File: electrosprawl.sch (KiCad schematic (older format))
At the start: 49 parts, among them J1 3.3v, J2 Conn_02x08_Counter_Clockwise, J3 Conn_02x06_Counter_Clockwise, J4 Conn_02x04_Counter_Clockwise, J5 Conn_02x08_Counter_Clockwise, J67 Conn_02x05_Counter_Clockwise, J7 VCC, J70 TXRX, J71 Micro_SD_Card_Det, J74 USB_B_Micro, SW1 Reset, U2 samd51p20, U5 LM1117-3.3, Y1 Crystal

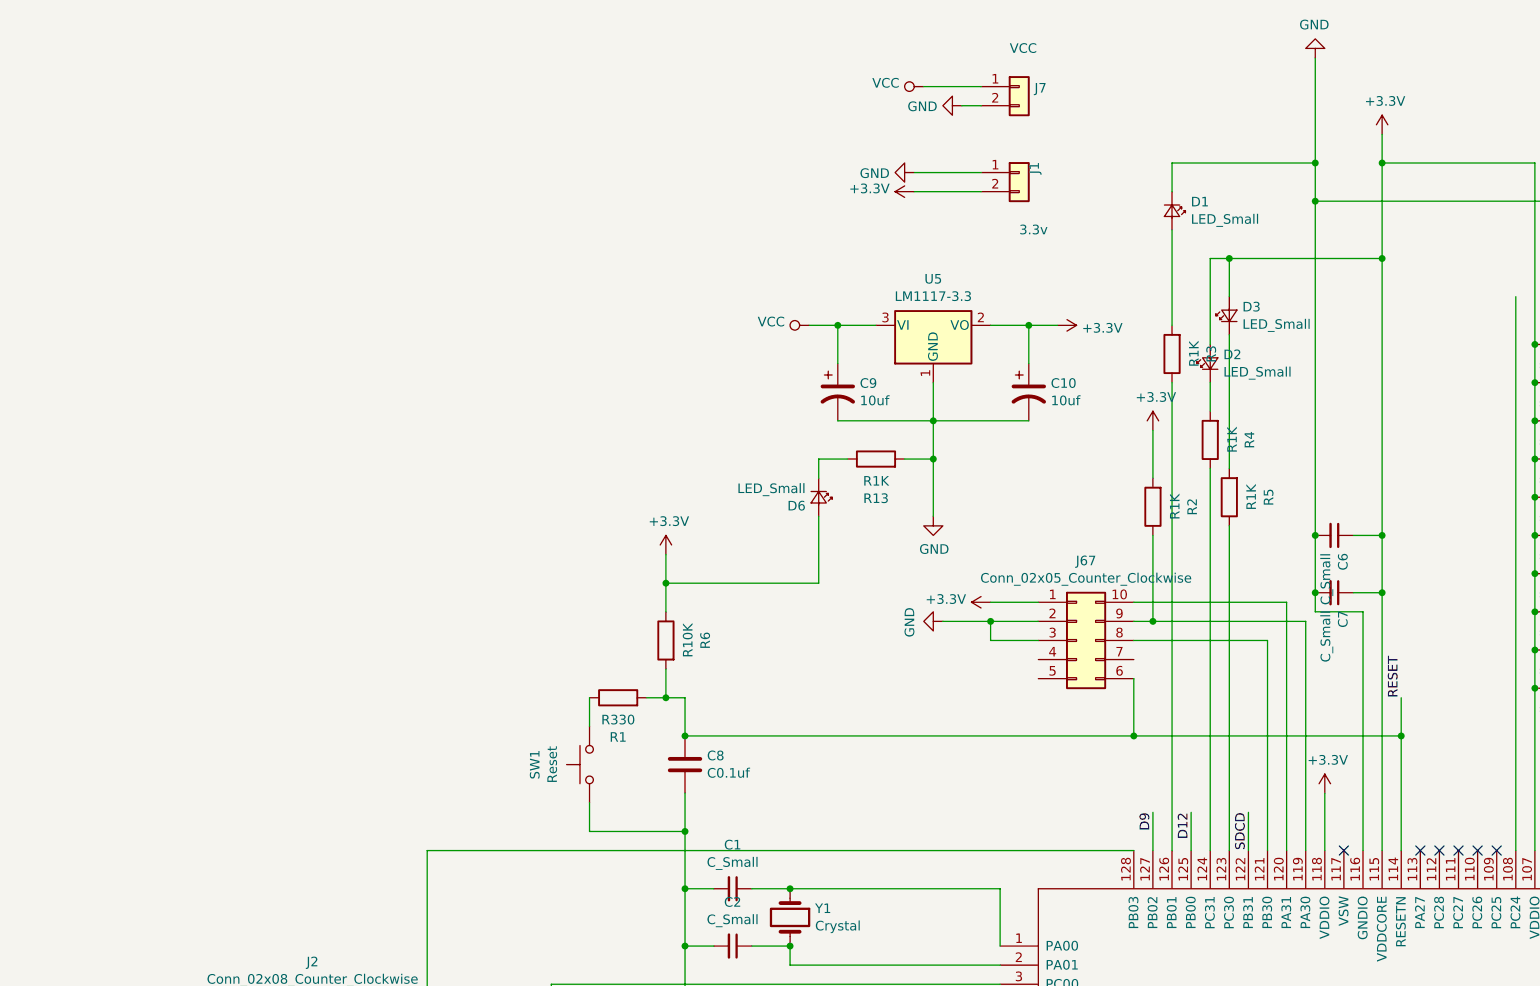
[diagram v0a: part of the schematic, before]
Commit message: add rgb led
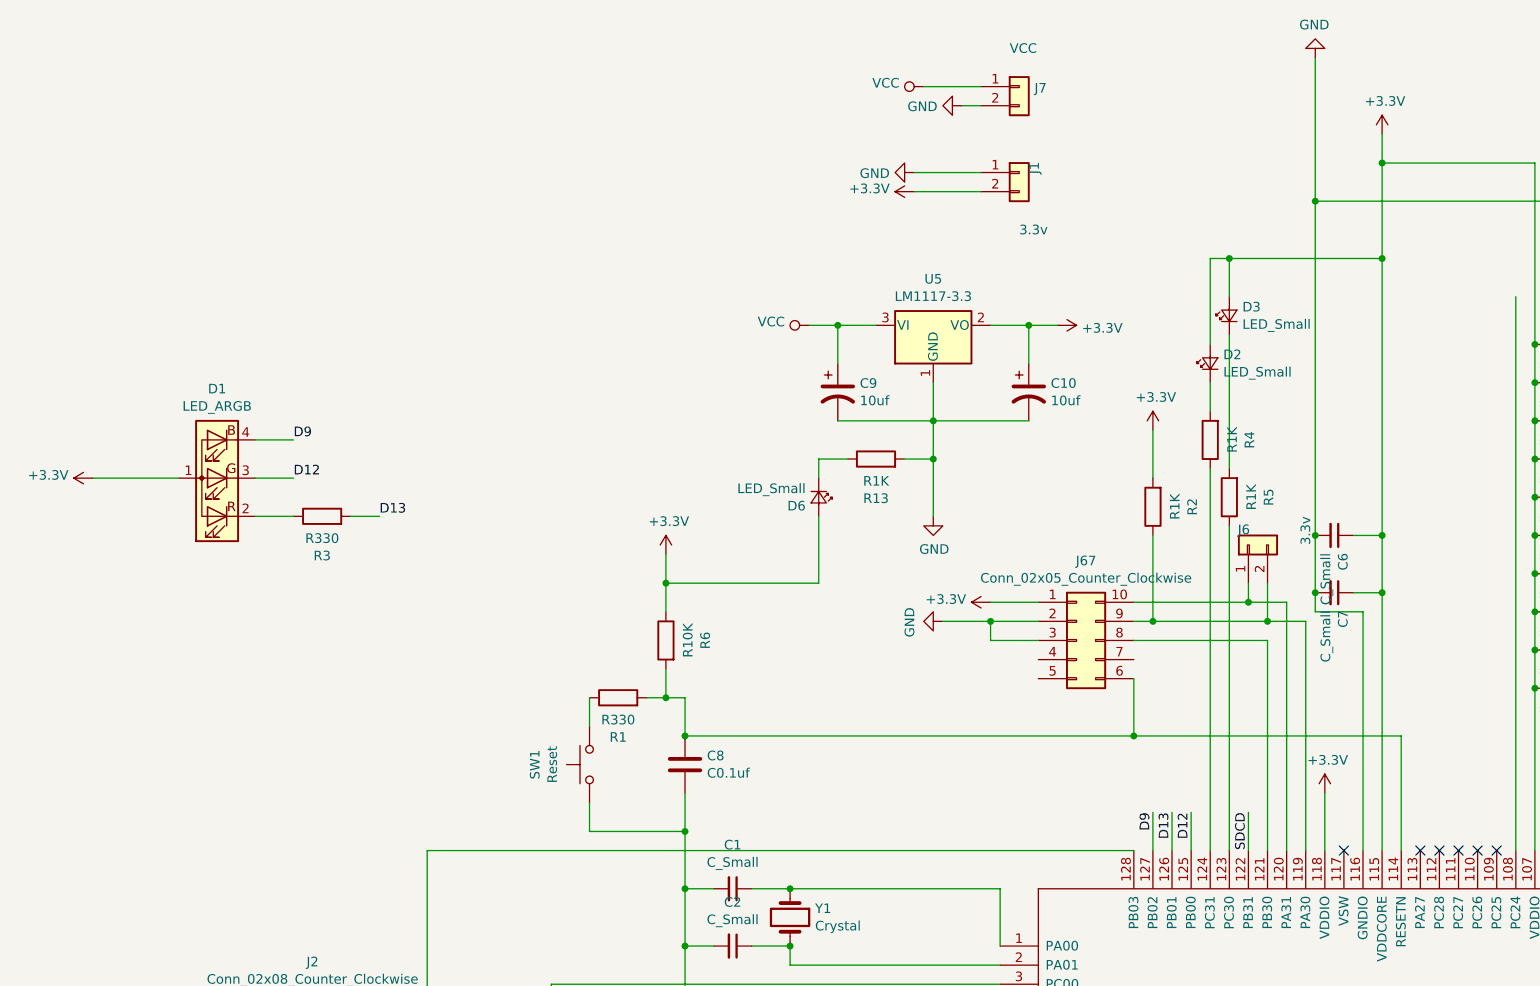
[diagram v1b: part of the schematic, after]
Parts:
- removed D1: LED_Small, LED_SMD:LED_0603_1608Metric, symbol Device:LED_Small
- added D1: LED_ARGB, LED_SMD:LED_RGB_5050-6, symbol Device:LED_ARGB
- added J6: 3.3v, Connector_PinHeader_2.54mm:PinHeader_1x02_P2.54mm_Vertical, symbol Connector_Generic:Conn_01x02
- R3: value R1K -> R330
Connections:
- net +3V3: now also D1.1 (A)
- net D12: now also D1.3 (GK)
- net D9: now also D1.4 (BK)
- net at J67.9 (Pin_9), R2.1, U2.119 (PA30): now also J6.2 (Pin_2)
- net at J67.10 (Pin_10), U2.120 (PA31): now also J6.1 (Pin_1)
- net at R3.1: now also D1.2 (RK); no longer U2.126 (PB01)
- net D13: now reaches R3.2
- net D13: now also U2.126 (PB01)
- net RESET: no longer names the net of C8.1, J67.6 (Pin_6), R1.2, R6.2, U2.114 (RESETN)

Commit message: update layout
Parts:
- added U?: ISO1050DUB, Package_SO:SOP-8_6.62x9.15mm_P2.54mm, symbol Interface_CAN_LIN:ISO1050DUB
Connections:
- net +3V3: no longer J74.1 (VBUS)
- new net +5V: J74.1 (VBUS)
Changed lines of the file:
@@
 EESchema Schematic File Version 4
-LIBS:electrosprawl-cache
+LIBS:test-cache
 EELAYER 29 0
 EELAYER END
@@
 $EndComp
 $Comp
-L power:+3.3V #PWR0108
-U 1 1 5C88E71E
-P 24650 6950
-F 0 "#PWR0108" H 24650 6800 50  0001 C CNN
-F 1 "+3.3V" V 24665 7078 50  0000 L CNN
-F 2 "" H 24650 6950 50  0001 C CNN
-F 3 "" H 24650 6950 50  0001 C CNN
-	1    24650 6950
-	0    -1   -1   0
-$EndComp
-$Comp
 L power:GND #PWR0118
 U 1 1 5DBD1EAA
@@
 Wire Wire Line
 	13700 5300 13850 5300
+$Comp
+L power:+5V #PWR?
+U 1 1 5CE30BE4
+P 24650 6950
+F 0 "#PWR?" H 24650 6800 50  0001 C CNN
+F 1 "+5V" V 24665 7078 50  0000 L CNN
+F 2 "" H 24650 6950 50  0001 C CNN
+F 3 "" H 24650 6950 50  0001 C CNN
+	1    24650 6950
+	0    -1   -1   0
+$EndComp
+$Comp
+L Interface_CAN_LIN:ISO1050DUB U?
+U 1 1 5CEF30CF
+P 20500 14150
+F 0 "U?" H 20500 14517 50  0000 C CNN
+F 1 "ISO1050DUB" H 20500 14426 50  0000 C CNN
+F 2 "Package_SO:SOP-8_6.62x9.15mm_P2.54mm" H 20500 13800 50  0001 C CIN
+F 3 "http://www.ti.com/lit/ds/symlink/iso1050.pdf" H 20500 14100 50  0001 C CNN
+	1    20500 14150
+	1    0    0    -1
+$EndComp
 $EndSCHEMATC

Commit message: update redesign
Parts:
- removed J1: 3.3v, Connector_PinHeader_2.54mm:PinHeader_1x02_P2.54mm_Vertical, symbol Connector_Generic:Conn_01x02
- removed J3: Conn_02x06_Counter_Clockwise, Connector_PinHeader_2.54mm:PinHeader_2x06_P2.54mm_Vertical, symbol Connector_Generic:Conn_02x06_Counter_Clockwise
- removed J4: Conn_02x04_Counter_Clockwise, Connector_PinHeader_2.54mm:PinHeader_2x04_P2.54mm_Vertical, symbol Connector_Generic:Conn_02x04_Counter_Clockwise
- removed J71: Micro_SD_Card_Det, Connector_Card:microSD_HC_Hirose_DM3D-SF, symbol electrosprawl-rescue:Micro_SD_Card_Det-Connector
- removed U2: samd51p20, Package_QFP:TQFP-128_14x14mm_P0.4mm, symbol electrosprawl-rescue:samd51p20-samd51p20
- removed U?: ISO1050DUB, Package_SO:SOP-8_6.62x9.15mm_P2.54mm, symbol Interface_CAN_LIN:ISO1050DUB
- added J1: Micro_SD_Card_Det, Connector_Card:microSD_HC_Hirose_DM3D-SF, symbol Connector:Micro_SD_Card_Det
- added J3: Conn_02x16_Odd_Even, Connector_PinHeader_2.54mm:PinHeader_2x16_P2.54mm_Vertical, symbol Connector_Generic:Conn_02x16_Odd_Even
- added U1: samd51p20, Package_QFP:TQFP-128_14x14mm_P0.4mm, symbol samd51p20:samd51p20
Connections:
- net +: now also U1.95 (PA25)
- net +3V3: now also J1.4 (VDD), J3.1 (Pin_1), J3.3 (Pin_3), U1.107 (VDDIO), U1.115 (VDDCORE), U1.118 (VDDIO), U1.15 (VDDANA), U1.26 (VDDANA), U1.32 (VDDIOB), U1.46 (VDDIO), U1.54 (VDDIO), U1.6 (VDDANA), U1.65 (VDDIO), U1.79 (VDDIO), U1.91 (VDDIO), U1.97 (VDDIO)
- net -: now also U1.94 (PA24)
- net D10: now also U1.98 (PB22)
- net D11: now also U1.99 (PB23)
- net D12: now also U1.125 (PB00)
- net D13: now also U1.126 (PB01)
- net D9: now also U1.127 (PB02)
- net GND: now also J1.11 (SHIELD), J1.6 (VSS), J3.2 (Pin_2), J3.29 (Pin_29), J3.31 (Pin_31), J3.4 (Pin_4), U1.106 (GND), U1.116 (GNDIO), U1.14 (GNDANA), U1.25 (GNDANA), U1.31 (GND), U1.38 (GND), U1.45 (GND), U1.5 (GND), U1.53 (GND), U1.64 (GND), U1.78 (GND), U1.90 (GND), U1.96 (GND)
- net SDCD: now also J1.10 (DET_A), U1.122 (PB31)
- net at C8.1, J67.6 (Pin_6), R1.2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: now also U1.114 (RESETN)
- net at C1.1, Y1.1: now also U1.1 (PA00)
- net at J70.2 (Pin_2): now also U1.100 (PB24)
- net at J70.1 (Pin_1): now also U1.101 (PB25)
- net at J2.10 (Pin_10): now also U1.11 (PB04)
- net at J6.2 (Pin_2), J67.9 (Pin_9), R2.1: now also U1.119 (PA30)
- net at J2.9 (Pin_9): now also U1.12 (PB05)
- net at J6.1 (Pin_1), J67.10 (Pin_10): now also U1.120 (PA31)
- net at J67.8 (Pin_8): now also U1.121 (PB30)
- net at R5.1: now also U1.123 (PC30)
- net at R4.1: now also U1.124 (PC31)
- net at J2.16 (Pin_16): now also U1.128 (PB03)
- net at J2.8 (Pin_8): now also U1.17 (PB06)
- net at J2.7 (Pin_7): now also U1.18 (PB07)
- net at J2.6 (Pin_6): now also U1.19 (PB08)
- net at C2.1, Y1.2: now also U1.2 (PA01)
- net at J2.5 (Pin_5): now also U1.20 (PB09)
- net at J2.4 (Pin_4): now also U1.21 (PA04)
- net at J2.3 (Pin_3): now also U1.22 (PA05)
- net at J2.2 (Pin_2): now also U1.23 (PA06)
- net at J2.1 (Pin_1): now also U1.24 (PA07)
- net at J2.15 (Pin_15): now also U1.3 (PC00)
- net at J2.14 (Pin_14): now also U1.4 (PC01)
- net at J5.16 (Pin_16): now also U1.66 (PA16)
- net at J5.15 (Pin_15): now also U1.67 (PA17)
- net at J5.14 (Pin_14): now also U1.68 (PA18)
- net at J5.13 (Pin_13): now also U1.69 (PA19)
- net at J2.13 (Pin_13): now also U1.7 (PC02)
- net at J5.12 (Pin_12): now also U1.72 (PC18)
- net at J5.11 (Pin_11): now also U1.73 (PC19)
- net at J5.10 (Pin_10): now also U1.74 (PC20)
- net at J5.9 (Pin_9): now also U1.75 (PC21)
- net at J2.12 (Pin_12): now also U1.8 (PC03)
- net at J5.8 (Pin_8): now also U1.84 (PB18)
- net at J5.7 (Pin_7): now also U1.85 (PB19)
- net at J5.6 (Pin_6): now also U1.86 (PB20)
- net at J5.5 (Pin_5): now also U1.87 (PB21)
- net at J5.4 (Pin_4): now also U1.88 (PA20)
- net at J5.3 (Pin_3): now also U1.89 (PA21)
- net at J2.11 (Pin_11): now also U1.9 (PA02)
- net at J5.2 (Pin_2): now also U1.92 (PA22)
- net at J5.1 (Pin_1): now also U1.93 (PA23)
- new net: J1.7 (DAT0), U1.102 (PB26)
- new net: J1.5 (CLK), U1.103 (PC24)
- new net: J1.3 (CMD), U1.104 (PB28)
- new net: J1.8 (DAT1), U1.105 (PB29)
- new net: J3.24 (Pin_24), U1.27 (PC04)
- new net: J3.22 (Pin_22), U1.28 (PC05)
- new net: J3.28 (Pin_28), U1.29 (PC06)
- new net: J3.26 (Pin_26), U1.30 (PC07)
- new net: J3.30 (Pin_30), U1.33 (PA08)
- new net: J3.32 (Pin_32), U1.34 (PA09)
- new net: J3.27 (Pin_27), U1.35 (PA10)
- new net: J3.25 (Pin_25), U1.36 (PA11)
- new net: J3.23 (Pin_23), U1.37 (VDDIOB)
- new net: J3.21 (Pin_21), U1.39 (PB10)
- new net: J3.19 (Pin_19), U1.40 (PB11)
- new net: J3.17 (Pin_17), U1.41 (PB12)
- new net: J3.15 (Pin_15), U1.42 (PB13)
- new net: J3.13 (Pin_13), U1.43 (PB14)
- new net: J3.11 (Pin_11), U1.44 (PB15)
- new net: J3.9 (Pin_9), U1.47 (PD08)
- new net: J3.7 (Pin_7), U1.48 (PD09)
- new net: J3.5 (Pin_5), U1.49 (PD10)
- new net: J3.20 (Pin_20), U1.56 (PC12)
- new net: J3.18 (Pin_18), U1.57 (PC13)
- new net: J3.16 (Pin_16), U1.58 (PC14)
- new net: J3.14 (Pin_14), U1.59 (PC15)
- new net: J3.12 (Pin_12), U1.60 (PA12)
- new net: J3.10 (Pin_10), U1.61 (PA13)
- new net: J3.8 (Pin_8), U1.62 (PA14)
- new net: J3.6 (Pin_6), U1.63 (PA15)

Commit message: update redesign
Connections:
- wire segments 364 -> 321
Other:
- moved on the sheet: J3

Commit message: update redesign
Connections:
- wire segments 321 -> 344
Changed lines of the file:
@@
 	-1   0    0    1
 $EndComp
-Wire Wire Line
-	16450 10650 16450 15100
 $Comp
 L power:GND #PWR0125
@@
 	21600 10650 21900 10650
 Wire Wire Line
-	20800 11150 20800 12550
-Wire Wire Line
-	20700 11150 20700 12900
-Wire Wire Line
-	20600 11150 20600 12850
-Wire Wire Line
-	20500 11150 20500 12800
-Wire Wire Line
 	17100 8050 15800 8050
-Wire Wire Line
-	20400 11150 20400 12750
-Wire Wire Line
-	20300 11150 20300 12700
-Wire Wire Line
-	20200 11150 20200 12650
-Wire Wire Line
-	20100 11150 20100 12600
 Wire Wire Line
 	19900 11150 19900 11350
@@
 Wire Wire Line
 	20900 11150 20900 13200
-Wire Wire Line
-	18300 11350 18400 11350
-Wire Wire Line
-	18400 11350 18400 11150
-Wire Wire Line
-	18500 11150 18500 11400
-Wire Wire Line
-	18400 11400 18500 11400
 $Comp
 L samd51p20:samd51p20 U1
@@
 $EndComp
 Wire Wire Line
-	18400 12050 18400 11400
-Wire Wire Line
-	18300 12050 18300 11350
-Wire Wire Line
-	18200 11150 18200 12050
+	16650 11950 17400 11950
+Wire Wire Line
+	16700 11900 17500 11900
+Wire Wire Line
+	16550 11850 17600 11850
+Wire Wire Line
+	16600 11800 17700 11800
+Wire Wire Line
+	20200 11150 20200 12950
+Wire Wire Line
+	20100 11150 20100 12900
+Wire Wire Line
+	18200 12900 20100 12900
+Wire Wire Line
+	18300 12950 20200 12950
+Wire Wire Line
+	18400 13000 20300 13000
+Wire Wire Line
+	20300 11150 20300 13000
+Wire Wire Line
+	18500 13050 20400 13050
+Wire Wire Line
+	20400 11150 20400 13050
+Wire Wire Line
+	18600 13100 20500 13100
+Wire Wire Line
+	20500 11150 20500 13100
+Wire Wire Line
+	18700 13150 20600 13150
+Wire Wire Line
+	20600 11150 20600 13150
+Wire Wire Line
+	17400 11950 17400 12050
+Wire Wire Line
+	17500 11900 17500 12050
+Wire Wire Line
+	17600 11850 17600 12050
+Wire Wire Line
+	17700 11800 17700 12050
+Wire Wire Line
+	20700 11150 20700 13200
+Wire Wire Line
+	18800 13200 20700 13200
+Wire Wire Line
+	18800 12550 18800 13200
+Wire Wire Line
+	18700 12550 18700 13150
+Wire Wire Line
+	18600 12550 18600 13100
+Wire Wire Line
+	18500 12550 18500 13050
+Wire Wire Line
+	18400 12550 18400 13000
+Wire Wire Line
+	18300 12550 18300 12950
+Wire Wire Line
+	18200 12550 18200 12900
+Wire Wire Line
+	18900 12550 18900 12850
+Wire Wire Line
+	18900 12850 20800 12850
+Wire Wire Line
+	20800 11150 20800 12850
+Wire Wire Line
+	16450 10650 16450 11350
+Wire Wire Line
+	16450 11350 18200 11350
+Wire Wire Line
+	18200 11350 18200 11150
+Connection ~ 16450 11350
+Wire Wire Line
+	16450 11350 16450 15100
+Wire Wire Line
+	18400 11150 18400 11400
+Wire Wire Line
+	18200 11400 18400 11400
+Wire Wire Line
+	18500 11150 18500 11450
+Wire Wire Line
+	18300 11450 18500 11450
+Wire Wire Line
+	18600 11150 18600 11500
+Wire Wire Line
+	18400 11500 18600 11500
+Wire Wire Line
+	18700 11150 18700 11550
+Wire Wire Line
+	18500 11550 18700 11550
+Wire Wire Line
+	18500 12050 18500 11550
+Wire Wire Line
+	18400 12050 18400 11500
+Wire Wire Line
+	18300 11450 18300 12050
+Wire Wire Line
+	18200 12050 18200 11400
 Wire Wire Line
 	18100 11150 18100 12050
@@
 $EndComp
 Wire Wire Line
-	18500 12050 18500 11450
-Wire Wire Line
-	18500 11450 18600 11450
-Wire Wire Line
-	18600 11450 18600 11150
-Wire Wire Line
-	18600 12050 18600 11500
-Wire Wire Line
-	18600 11500 18700 11500
-Wire Wire Line
-	18700 11500 18700 11150
-Wire Wire Line
-	18800 11150 18800 11550
-Wire Wire Line
-	18800 11550 18700 11550
-Wire Wire Line
-	18700 11550 18700 12050
-Wire Wire Line
-	18900 11150 18900 11800
-Wire Wire Line
-	18900 11800 18800 11800
-Wire Wire Line
-	18800 11800 18800 12050
-Wire Wire Line
-	19200 11950 18900 11950
-Wire Wire Line
-	18900 11950 18900 12050
-Wire Wire Line
-	19200 11950 19200 11150
+	18600 12050 18600 11600
+Wire Wire Line
+	18600 11600 18800 11600
+Wire Wire Line
+	18800 11150 18800 11600
+Wire Wire Line
+	18900 11150 18900 11650
+Wire Wire Line
+	18900 11650 18700 11650
+Wire Wire Line
+	18700 11650 18700 12050
 $EndSCHEMATC

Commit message: update
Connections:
- net +3V3: now also J3.1 (Pin_1), J3.3 (Pin_3)
- net GND: now also J3.18 (Pin_18), J3.20 (Pin_20), J3.22 (Pin_22), J3.24 (Pin_24), J3.26 (Pin_26), J3.28 (Pin_28), J3.30 (Pin_30), J3.32 (Pin_32)
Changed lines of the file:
@@
 	1    0    0    -1
-$EndComp
-$Comp
-L power:+3.3V #PWR0124
-U 1 1 5CF9225B
-P 19900 12150
-F 0 "#PWR0124" H 19900 12000 50  0001 C CNN
-F 1 "+3.3V" H 19900 12350 50  0000 C CNN
-F 2 "" H 19900 12150 50  0001 C CNN
-F 3 "" H 19900 12150 50  0001 C CNN
-	1    19900 12150
-	-1   0    0    1
 $EndComp
 Wire Wire Line
@@
 Connection ~ 19900 11350
 Wire Wire Line
-	19900 11350 19900 12150
-Wire Wire Line
 	20700 7050 20700 6850
 Wire Wire Line
@@
 Wire Wire Line
 	17800 11150 17800 12050
+Wire Wire Line
+	18600 12050 18600 11600
+Wire Wire Line
+	18600 11600 18800 11600
+Wire Wire Line
+	18800 11150 18800 11600
+Wire Wire Line
+	18900 11150 18900 11650
+Wire Wire Line
+	18900 11650 18700 11650
+Wire Wire Line
+	18700 11650 18700 12050
 $Comp
 L Connector_Generic:Conn_02x16_Odd_Even J3
@@
 	0    1    1    0
 $EndComp
-Wire Wire Line
-	18600 12050 18600 11600
-Wire Wire Line
-	18600 11600 18800 11600
-Wire Wire Line
-	18800 11150 18800 11600
-Wire Wire Line
-	18900 11150 18900 11650
-Wire Wire Line
-	18900 11650 18700 11650
-Wire Wire Line
-	18700 11650 18700 12050
+Connection ~ 17400 12550
+Wire Wire Line
+	17400 12550 17500 12550
+Connection ~ 17500 12550
+Wire Wire Line
+	17500 12550 17600 12550
+Connection ~ 17600 12550
+Wire Wire Line
+	17600 12550 17700 12550
+Connection ~ 17700 12550
+Wire Wire Line
+	17700 12550 17800 12550
+Connection ~ 17800 12550
+Wire Wire Line
+	17800 12550 17900 12550
+Connection ~ 17900 12550
+Wire Wire Line
+	17900 12550 18000 12550
+Connection ~ 18000 12550
+Wire Wire Line
+	18000 12550 18100 12550
+Wire Wire Line
+	17000 12550 17400 12550
+Wire Wire Line
+	19900 11350 19900 12050
+$Comp
+L power:+3.3V #PWR0124
+U 1 1 5CF9225B
+P 19900 12350
+F 0 "#PWR0124" H 19900 12200 50  0001 C CNN
+F 1 "+3.3V" H 19900 12550 50  0000 C CNN
+F 2 "" H 19900 12350 50  0001 C CNN
+F 3 "" H 19900 12350 50  0001 C CNN
+	1    19900 12350
+	-1   0    0    1
+$EndComp
+Wire Wire Line
+	18800 12050 18900 12050
+Connection ~ 19900 12050
+Wire Wire Line
+	19900 12050 19900 12350
+Connection ~ 18900 12050
+Wire Wire Line
+	18900 12050 19900 12050
+$Comp
+L power:GND #PWR?
+U 1 1 5F01DCED
+P 17000 12550
+F 0 "#PWR?" H 17000 12300 50  0001 C CNN
+F 1 "GND" V 17005 12422 50  0000 R CNN
+F 2 "" H 17000 12550 50  0001 C CNN
+F 3 "" H 17000 12550 50  0001 C CNN
+	1    17000 12550
+	0    1    1    0
+$EndComp
 $EndSCHEMATC

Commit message: update
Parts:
- H4: footprint MountingHole:MountingHole_3mm -> MountingHole:MountingHole_3mm_Pad_Via; symbol Mechanical:MountingHole -> Mechanical:MountingHole_Pad
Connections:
- net GND: now also H4.1
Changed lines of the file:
@@
-$EndComp
-$Comp
-L Mechanical:MountingHole H4
-U 1 1 5C6145C5
-P 13550 13600
-F 0 "H4" H 13650 13646 50  0000 L CNN
-F 1 "MountingHole" H 14100 13250 50  0000 L CNN
-F 2 "MountingHole:MountingHole_3mm" H 13550 13600 50  0001 C CNN
-F 3 "~" H 13550 13600 50  0001 C CNN
-	1    13550 13600
-	1    0    0    -1
 $EndComp
 $Comp
@@
 	18900 12050 19900 12050
 $Comp
-L power:GND #PWR?
+L power:GND #PWR0101
 U 1 1 5F01DCED
 P 17000 12550
-F 0 "#PWR?" H 17000 12300 50  0001 C CNN
+F 0 "#PWR0101" H 17000 12300 50  0001 C CNN
 F 1 "GND" V 17005 12422 50  0000 R CNN
 F 2 "" H 17000 12550 50  0001 C CNN
@@
 	0    1    1    0
 $EndComp
+$Comp
+L Mechanical:MountingHole_Pad H4
+U 1 1 5C6145C5
+P 13550 13550
+F 0 "H4" H 13650 13596 50  0000 L CNN
+F 1 "MountingHole" H 14100 13200 50  0000 L CNN
+F 2 "MountingHole:MountingHole_3mm_Pad_Via" H 13550 13550 50  0001 C CNN
+F 3 "~" H 13550 13550 50  0001 C CNN
+	1    13550 13550
+	-1   0    0    1
+$EndComp
+Wire Wire Line
+	13550 13300 13550 13450
+$Comp
+L power:GND #PWR0122
+U 1 1 5F5827B8
+P 13550 13300
+F 0 "#PWR0122" H 13550 13050 50  0001 C CNN
+F 1 "GND" V 13555 13172 50  0000 R CNN
+F 2 "" H 13550 13300 50  0001 C CNN
+F 3 "" H 13550 13300 50  0001 C CNN
+	1    13550 13300
+	-1   0    0    1
+$EndComp
 $EndSCHEMATC
